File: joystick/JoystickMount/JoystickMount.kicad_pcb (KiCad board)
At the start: 2 copper layers, 5 parts

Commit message: update joystick mount footprint
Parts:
- H1, H2, H3, H4: footprint MountingHole:MountingHole_2.2mm_M2_DIN965 -> ErgoCai.pretty:MountingHole_2.2mm_M2_DIN965
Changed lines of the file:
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@@
 	(net 4 "JT_B1")
 	(net 5 "ADC0")
-	(footprint "MountingHole:MountingHole_2.2mm_M2_DIN965"
+	(footprint "ErgoCai.pretty:MountingHole_2.2mm_M2_DIN965"
 		(layer "F.Cu")
 		(at -10.85 10.85)
@@
 		(property ki_fp_filters "MountingHole*")
 		(sheetname "/")
-		(sheetfile "Ps4Mount.kicad_sch")
+		(sheetfile "JoystickMount.kicad_sch")
 		(attr exclude_from_pos_files exclude_from_bom)
 		(fp_circle
@@
 		(embedded_fonts no)
 	)
-	(footprint "MountingHole:MountingHole_2.2mm_M2_DIN965"
+	(footprint "ErgoCai.pretty:MountingHole_2.2mm_M2_DIN965"
 		(layer "F.Cu")
 		(at 10.85 -10.85)
@@
 		(property ki_fp_filters "MountingHole*")
 		(sheetname "/")
-		(sheetfile "Ps4Mount.kicad_sch")
+		(sheetfile "JoystickMount.kicad_sch")
 		(attr exclude_from_pos_files exclude_from_bom)
 		(fp_circle
@@
 		)
 		(sheetname "/")
-		(sheetfile "Ps4Mount.kicad_sch")
+		(sheetfile "JoystickMount.kicad_sch")
 		(attr smd)
 		(fp_line
@@
 		)
 	)
-	(footprint "MountingHole:MountingHole_2.2mm_M2_DIN965"
+	(footprint "ErgoCai.pretty:MountingHole_2.2mm_M2_DIN965"
 		(layer "F.Cu")
 		(at 10.85 10.85)
@@
 		(property ki_fp_filters "MountingHole*")
 		(sheetname "/")
-		(sheetfile "Ps4Mount.kicad_sch")
+		(sheetfile "JoystickMount.kicad_sch")
 		(attr exclude_from_pos_files exclude_from_bom)
 		(fp_circle
@@
 		(embedded_fonts no)
 	)
-	(footprint "MountingHole:MountingHole_2.2mm_M2_DIN965"
+	(footprint "ErgoCai.pretty:MountingHole_2.2mm_M2_DIN965"
 		(layer "F.Cu")
 		(at -10.85 -10.85)
@@
 		(property ki_fp_filters "MountingHole*")
 		(sheetname "/")
-		(sheetfile "Ps4Mount.kicad_sch")
+		(sheetfile "JoystickMount.kicad_sch")
 		(attr exclude_from_pos_files exclude_from_bom)
 		(fp_circle

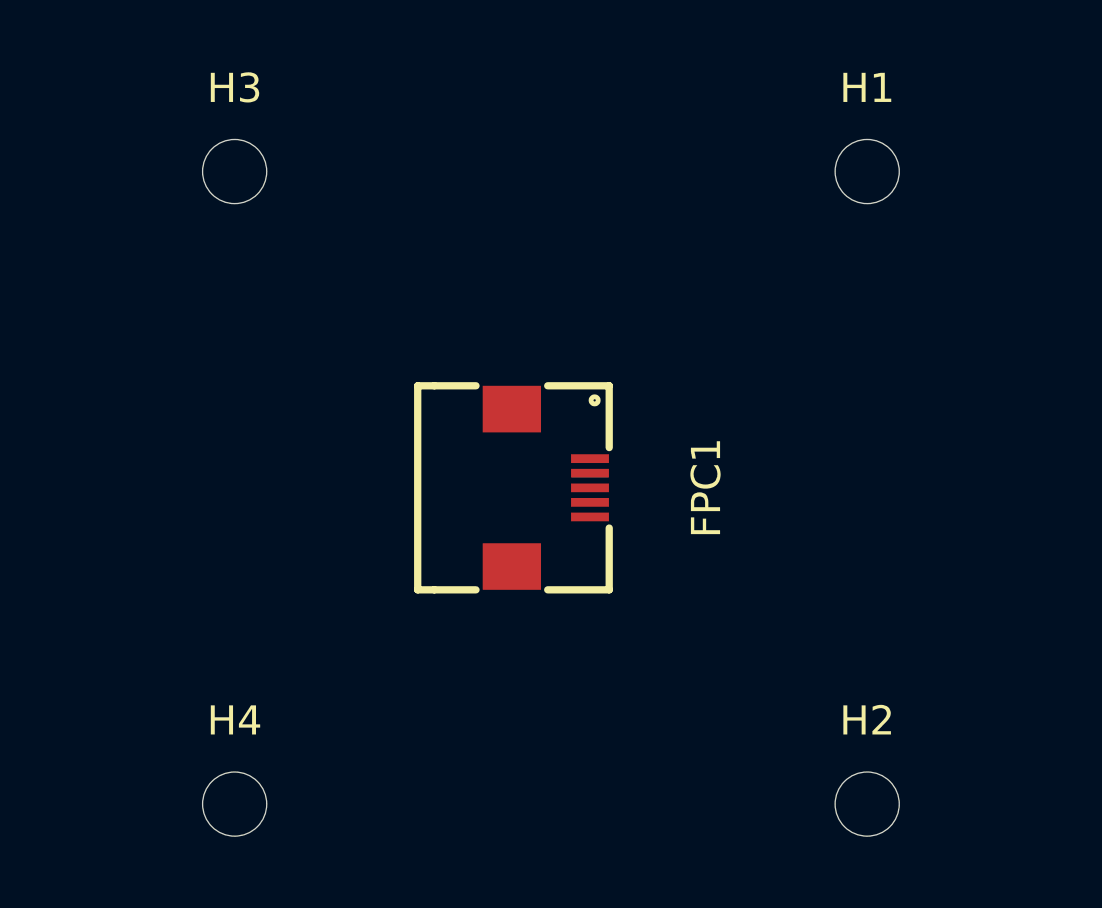
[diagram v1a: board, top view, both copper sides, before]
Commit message: update joystick mount footprint
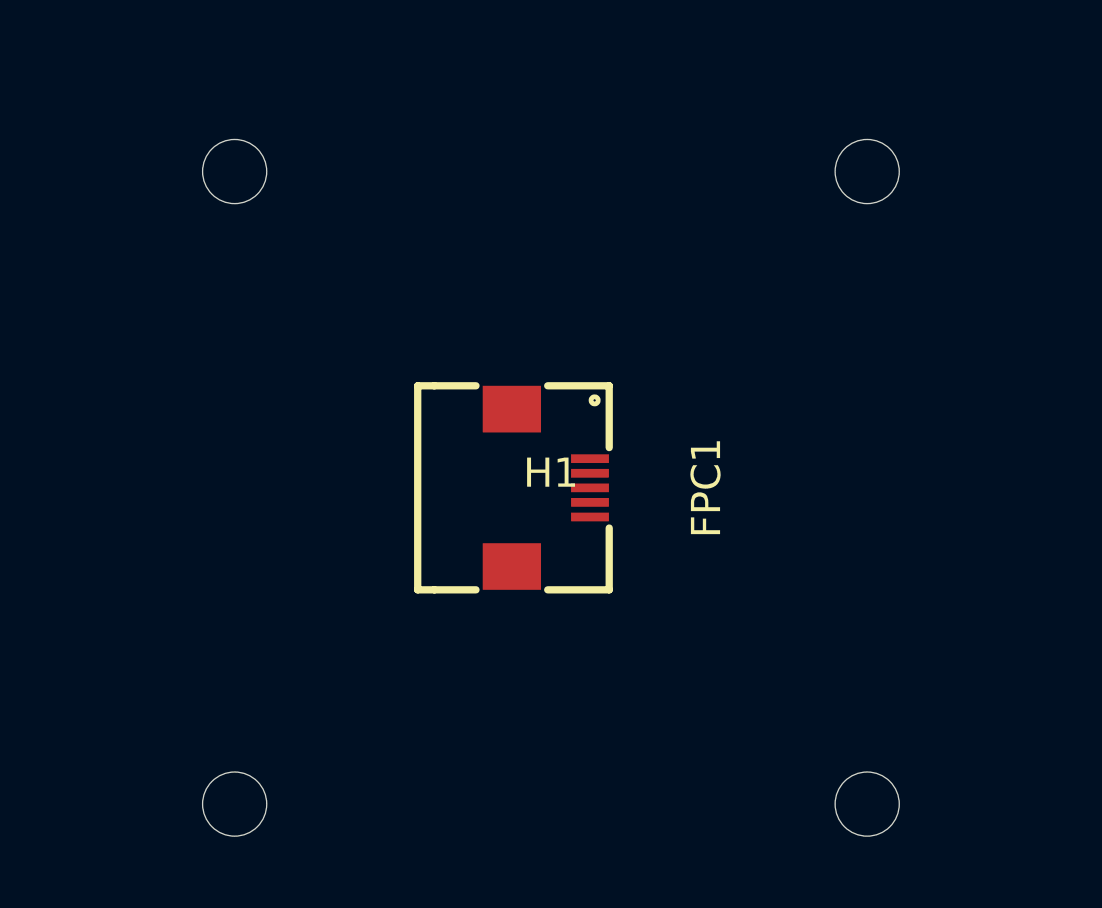
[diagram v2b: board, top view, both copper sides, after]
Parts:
- removed H2, H3, H4: MountingHole, ErgoCai.pretty:MountingHole_2.2mm_M2_DIN965
- H1: footprint ErgoCai.pretty:MountingHole_2.2mm_M2_DIN965 -> ErgoCai.pretty:Ps4JoystickMount
- moved H1 15.3 mm to (0.00, 0.00)

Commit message: add RGB WS2812B modules
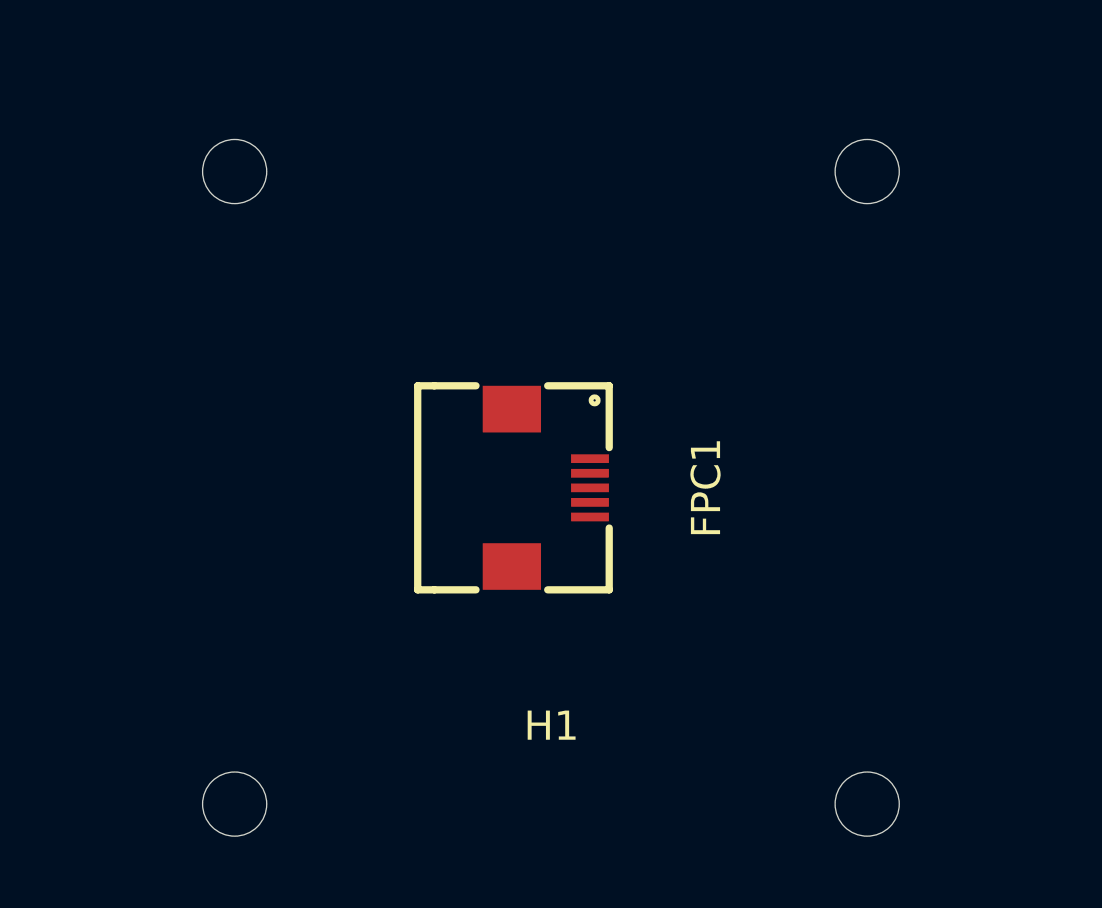
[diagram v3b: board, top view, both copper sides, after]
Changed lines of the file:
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@@
 		(at 0 0)
 		(property "Reference" "H1"
-			(at 0 -0.5 0)
+			(at 0.02 8.18 0)
 			(unlocked yes)
 			(layer "F.SilkS")
@@
 		)
 		(property "Value" "MountingHole"
-			(at 0 1 0)
+			(at -0.05 9.47 0)
 			(unlocked yes)
 			(layer "F.Fab")
@@
 		)
 		(fp_text user "${REFERENCE}"
-			(at 0 2.5 0)
+			(at -0.02 11.86 0)
 			(unlocked yes)
 			(layer "F.Fab")

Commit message: update joystick mount connector to JST ZH
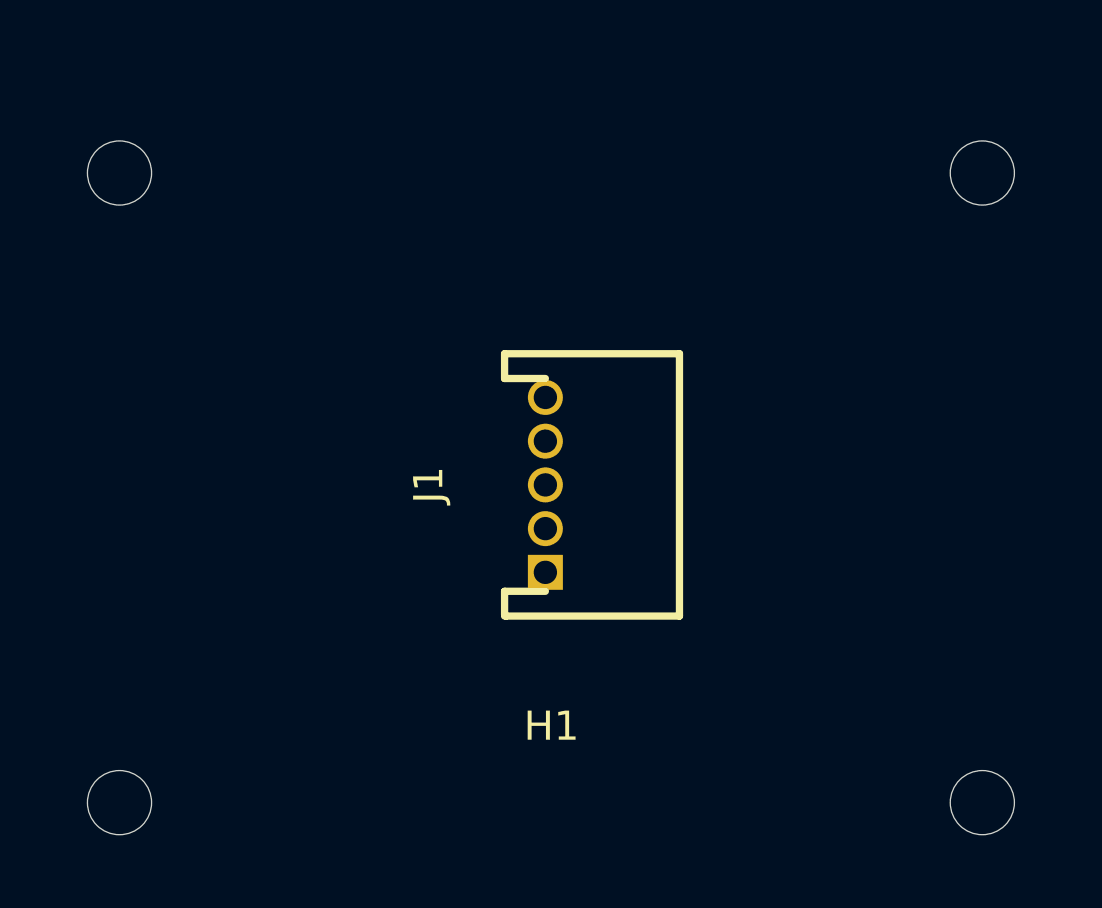
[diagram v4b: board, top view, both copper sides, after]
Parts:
- removed FPC1: AFC01-S05FCA-00, ErgoCai.pretty:FPC-SMD_AFC01-S05FCA-00
- added J1: Conn_01x05, ErgoCai.pretty:CONN-TH_S5B-ZR-LF-SN, F.Cu at (-0.19, -0.10)

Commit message: update joystick mount pos
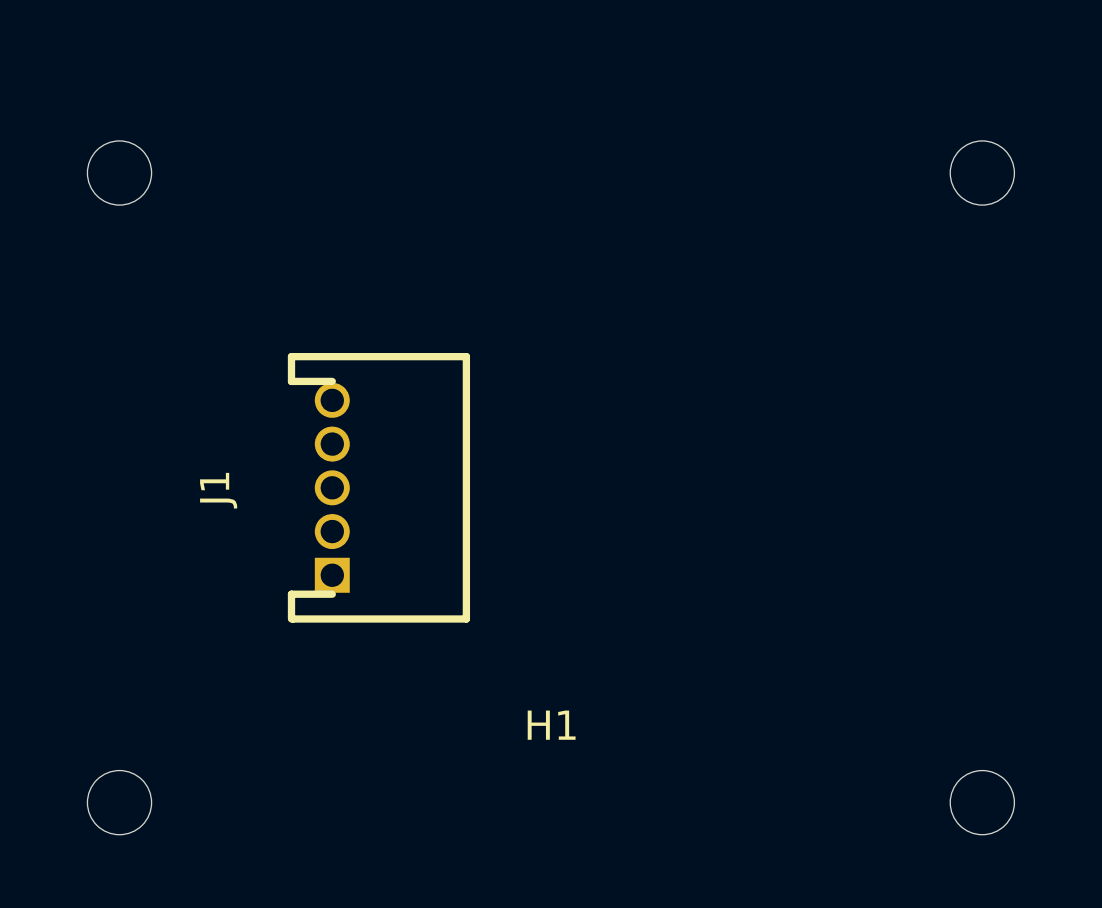
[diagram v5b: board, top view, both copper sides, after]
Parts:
- moved J1 7.31 mm to (-7.50, 0.00)
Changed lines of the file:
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@@
 	(footprint "ErgoCai.pretty:CONN-TH_S5B-ZR-LF-SN"
 		(layer "F.Cu")
-		(at -0.19 -0.1 90)
+		(at -7.5 0 90)
 		(property "Reference" "J1"
 			(at 0 -4 90)

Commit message: update joystick mount pos
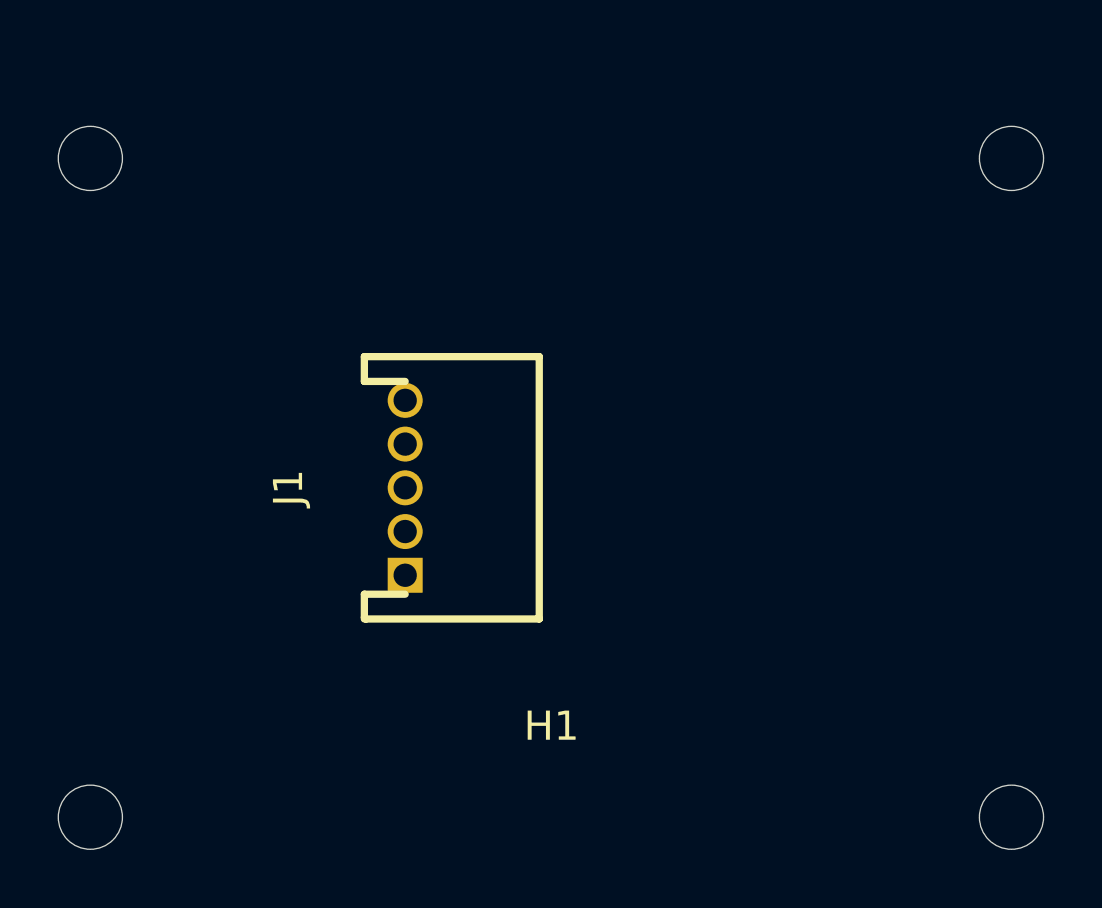
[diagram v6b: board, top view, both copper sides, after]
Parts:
- moved J1 2.50 mm to (-5.00, 0.00)
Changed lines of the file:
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@@
 		(attr exclude_from_pos_files exclude_from_bom)
 		(fp_line
-			(start -17 -13)
-			(end -17 13)
+			(start -18 -13.5)
+			(end -18 13.5)
 			(stroke
 				(width 0.1)
@@
 		)
 		(fp_line
-			(start -17 -13)
-			(end 17 -13)
+			(start -18 -13.5)
+			(end 18 -13.5)
 			(stroke
 				(width 0.1)
@@
 		)
 		(fp_line
-			(start -17 13)
-			(end 17 13)
+			(start -18 13.5)
+			(end 18 13.5)
 			(stroke
 				(width 0.1)
@@
 		)
 		(fp_line
-			(start 17 -13)
-			(end 17 13)
+			(start 18 -13.5)
+			(end 18 13.5)
 			(stroke
 				(width 0.1)
@@
 		)
 		(fp_circle
-			(center -14.8 -10.8)
-			(end -12.9 -10.8)
+			(center -15.8 -11.3)
+			(end -13.9 -11.3)
 			(stroke
 				(width 0.15)
@@
 		)
 		(fp_circle
-			(center -14.8 10.8)
-			(end -12.9 10.8)
+			(center -15.8 11.3)
+			(end -13.9 11.3)
 			(stroke
 				(width 0.15)
@@
 		)
 		(fp_circle
-			(center 14.8 -10.8)
-			(end 16.7 -10.8)
+			(center 15.8 -11.3)
+			(end 17.7 -11.3)
 			(stroke
 				(width 0.15)
@@
 		)
 		(fp_circle
-			(center 14.8 10.8)
-			(end 16.7 10.8)
+			(center 15.8 11.3)
+			(end 17.7 11.3)
 			(stroke
 				(width 0.15)
@@
 		)
 		(fp_circle
-			(center -14.8 -10.8)
-			(end -12.65 -10.8)
+			(center -15.8 -11.3)
+			(end -13.65 -11.3)
 			(stroke
 				(width 0.05)
@@
 		)
 		(fp_circle
-			(center -14.8 10.8)
-			(end -12.65 10.8)
+			(center -15.8 11.3)
+			(end -13.65 11.3)
 			(stroke
 				(width 0.05)
@@
 		)
 		(fp_circle
-			(center 14.8 -10.8)
-			(end 16.95 -10.8)
+			(center 15.8 -11.3)
+			(end 17.95 -11.3)
 			(stroke
 				(width 0.05)
@@
 		)
 		(fp_circle
-			(center 14.8 10.8)
-			(end 16.95 10.8)
+			(center 15.8 11.3)
+			(end 17.95 11.3)
 			(stroke
 				(width 0.05)
@@
 		)
 		(pad "" np_thru_hole circle
-			(at -14.8 -10.8)
+			(at -15.8 -11.3)
 			(size 2.2 2.2)
 			(drill 2.2)
@@
 		)
 		(pad "" np_thru_hole circle
-			(at -14.8 10.8)
+			(at -15.8 11.3)
 			(size 2.2 2.2)
 			(drill 2.2)
@@
 		)
 		(pad "" np_thru_hole circle
-			(at 14.8 -10.8)
+			(at 15.8 -11.3)
 			(size 2.2 2.2)
 			(drill 2.2)
@@
 		)
 		(pad "" np_thru_hole circle
-			(at 14.8 10.8)
+			(at 15.8 11.3)
 			(size 2.2 2.2)
 			(drill 2.2)
@@
 	(footprint "ErgoCai.pretty:CONN-TH_S5B-ZR-LF-SN"
 		(layer "F.Cu")
-		(at -7.5 0 90)
+		(at -5 0 90)
 		(property "Reference" "J1"
 			(at 0 -4 90)

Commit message: update to 3.3V tag
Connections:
- net VCC renamed 3.3V
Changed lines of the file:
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@@
 	(net 0 "")
 	(net 1 "GND")
-	(net 2 "VCC")
+	(net 2 "3.3V")
 	(net 3 "ADC_JT3")
 	(net 4 "ADC_JT1")
@@
 			(layers "*.Cu" "*.Mask")
 			(remove_unused_layers no)
-			(net 2 "VCC")
+			(net 2 "3.3V")
 			(pinfunction "Pin_2")
 			(pintype "passive")

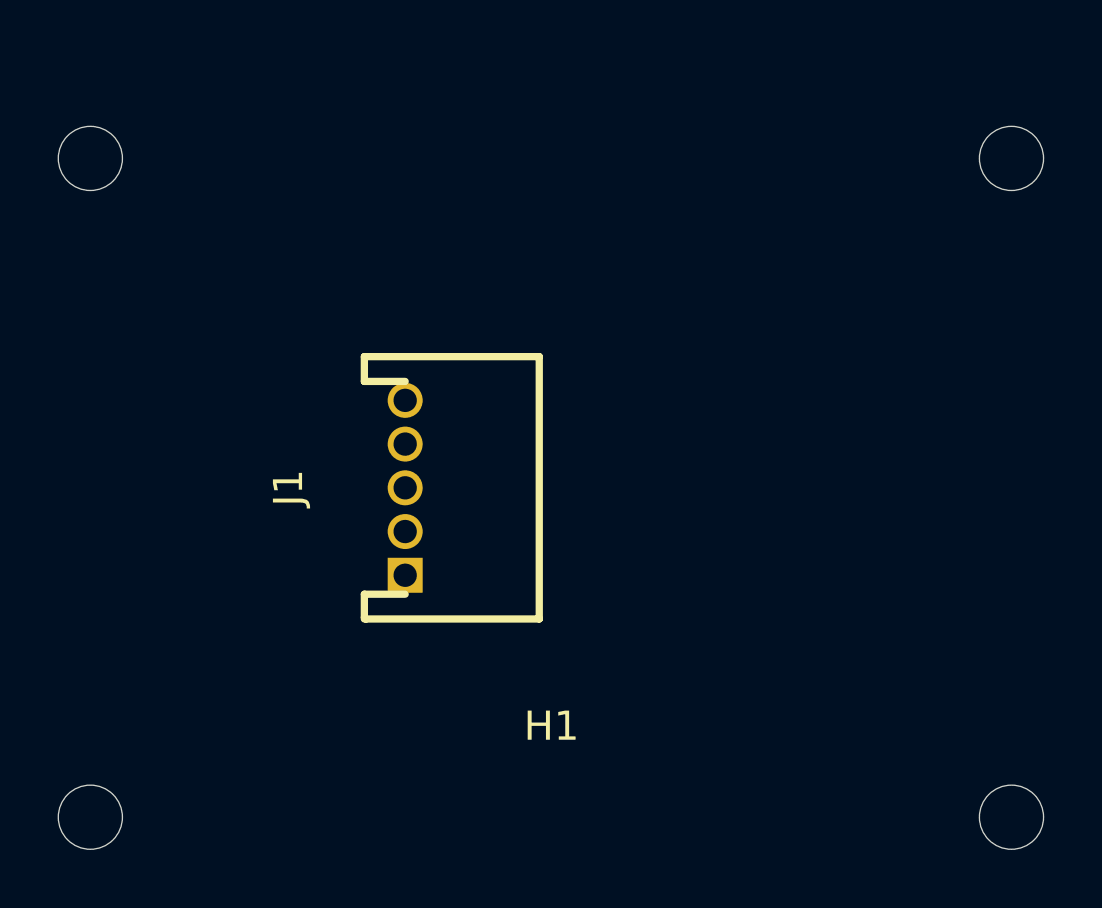
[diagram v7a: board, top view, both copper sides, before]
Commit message: update reference in joystick and e-paper
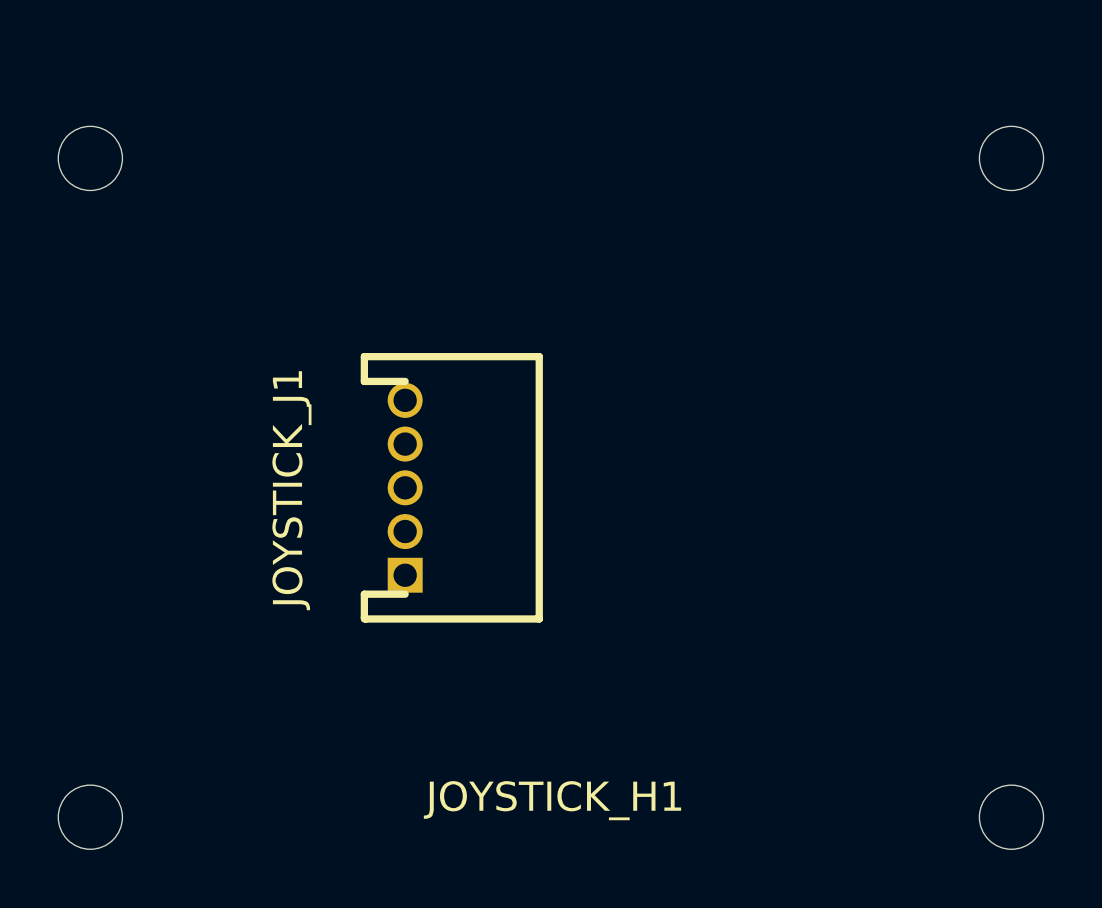
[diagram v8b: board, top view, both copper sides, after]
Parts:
- removed H1: MountingHole, ErgoCai.pretty:Ps4JoystickMount
- removed J1: Conn_01x05, ErgoCai.pretty:CONN-TH_S5B-ZR-LF-SN
- added JOYSTICK_H1: MountingHole, ErgoCai.pretty:Ps4JoystickMount, F.Cu at (0.00, 0.00)
- added JOYSTICK_J1: Conn_01x05, ErgoCai.pretty:CONN-TH_S5B-ZR-LF-SN, F.Cu at (-5.00, 0.00)
